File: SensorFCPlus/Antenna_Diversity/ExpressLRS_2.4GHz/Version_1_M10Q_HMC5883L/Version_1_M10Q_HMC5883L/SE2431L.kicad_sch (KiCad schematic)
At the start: 8 parts, among them U7 SE2431L-R

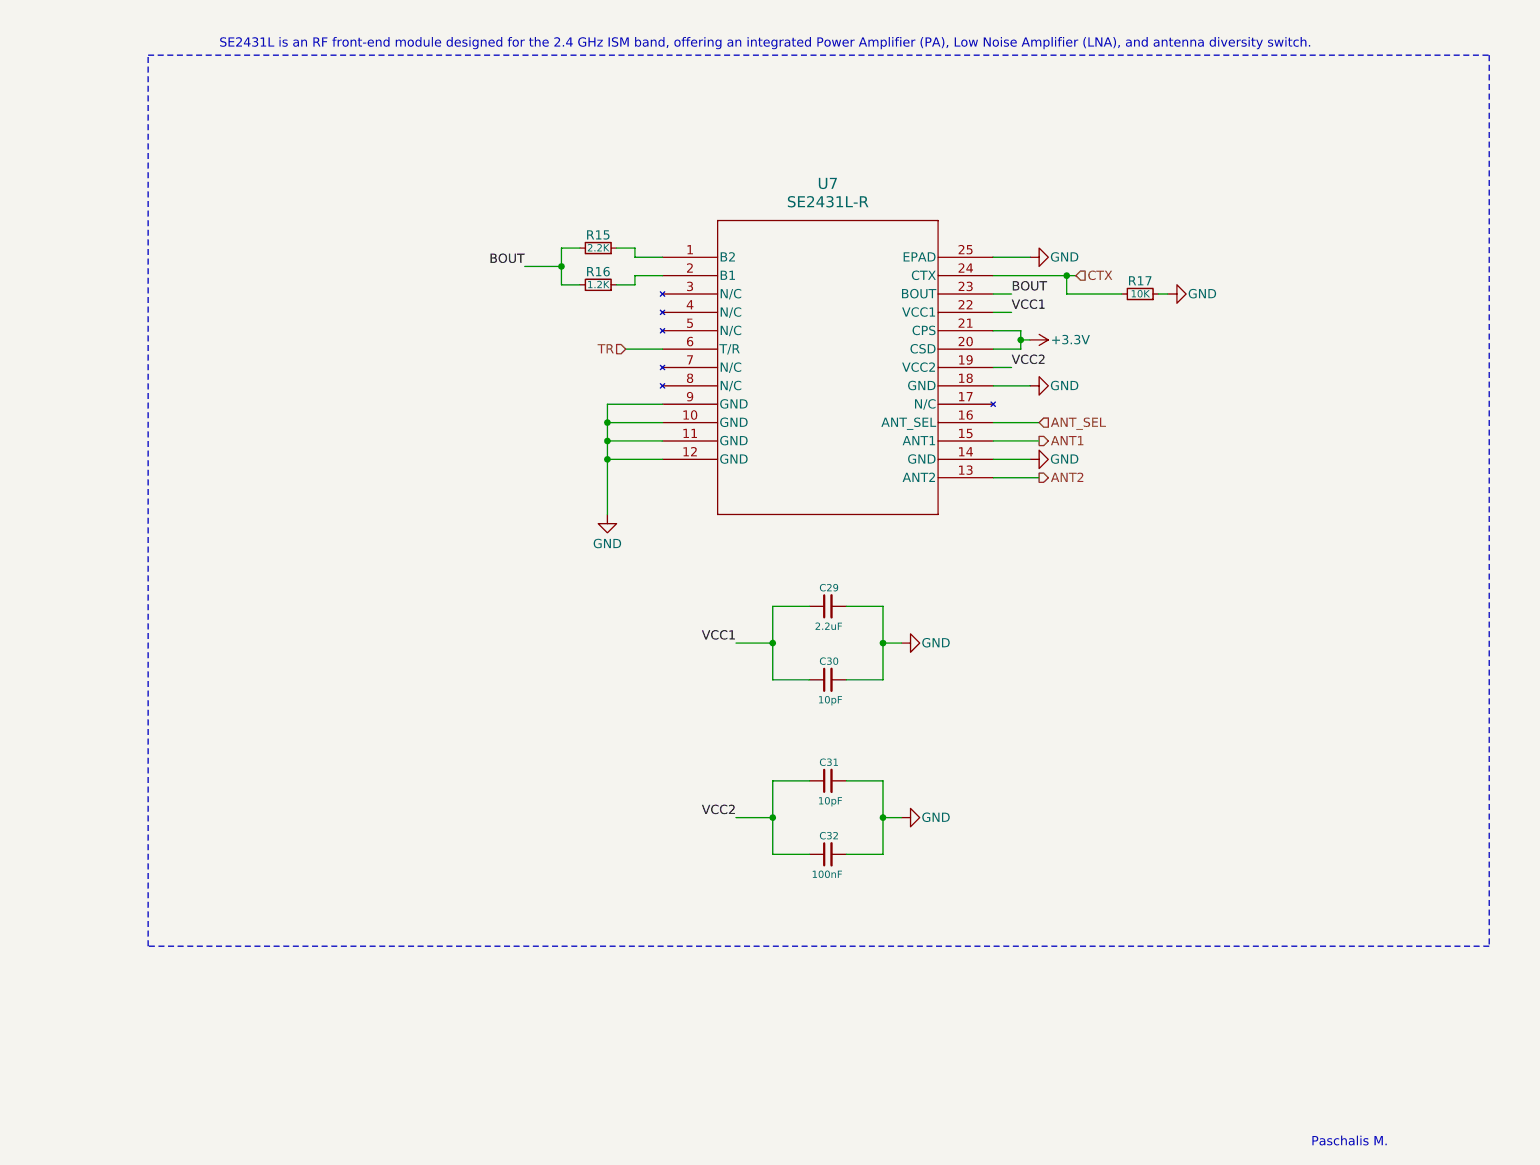
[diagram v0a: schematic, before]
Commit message: Updated README and V1 M10Q HMC5883L KiCad files, added documentation and media
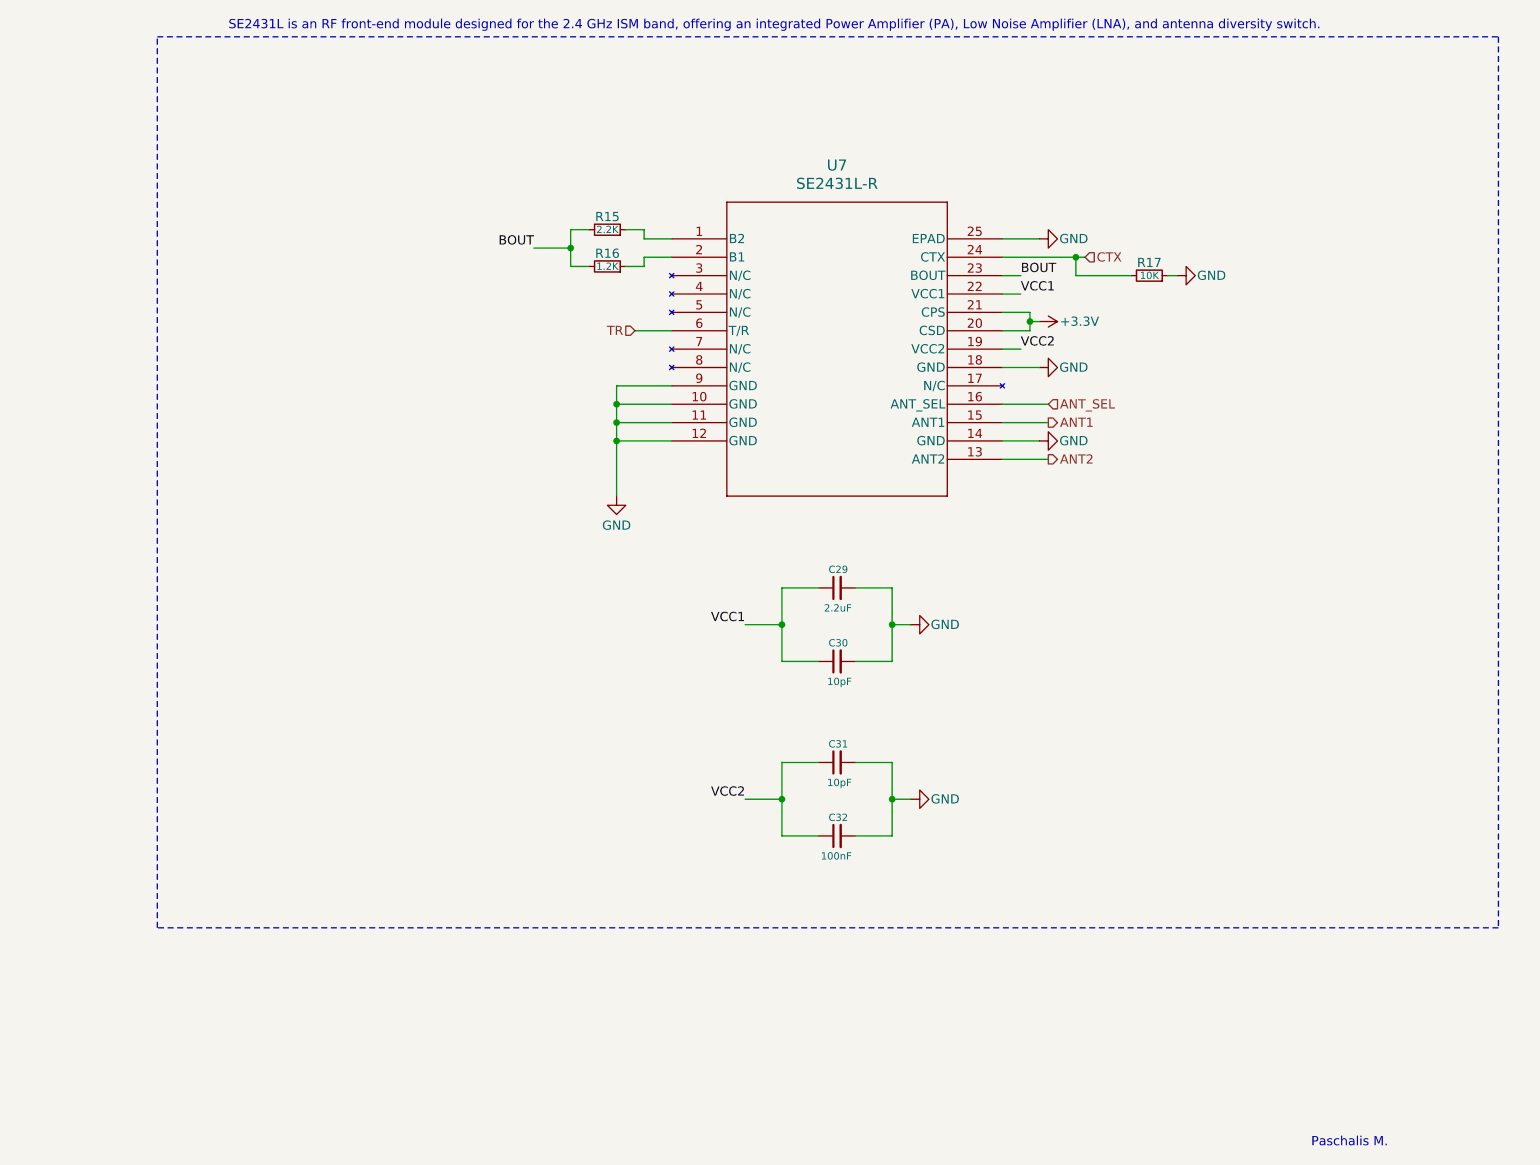
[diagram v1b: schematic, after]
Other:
- title: (none) -> SE2431L
